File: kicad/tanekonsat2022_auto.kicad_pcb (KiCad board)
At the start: 2 copper layers, 79 x 68 mm, 102 parts, among them IC1 W25Q128JVSIQ, IC2 ADP3338AKCZ-3.3-RL, IC4 TESEO-LIV3F, IC5 CGGBPD.25.A, IC6 MAX2641EUT+T, IC7 TB67H450FNG,EL, IC8 TB67H450FNG,EL, J1 Conn_01x02_Male, J10 Conn_01x05_Female, J11 Conn_01x02_Female, J2 USB_B_Micro, J3 Conn_01x02_Male, J4 Conn_01x02_Male, J5 Conn_01x04_Male, J6 Conn_01x04_Male, J7 Conn_01x04_Female, J8 Conn_01x02_Female, J9 Conn_01x05_Female, M1 Motor_DC, M2 Motor_DC, Q1 Q_NMOS_DGS, Q2 Q_NMOS_DGS, Q7 Q_NMOS_DGS, SW1 SW_DIP_x01, U1 RP2040, U2 CR1025, U5 LT6106, U6 Opamp_Dual, Y1 SIT2001BI-S2-33E-12.000000D, Y2 FC-135_32.768KHz_7pF_+_-20ppm

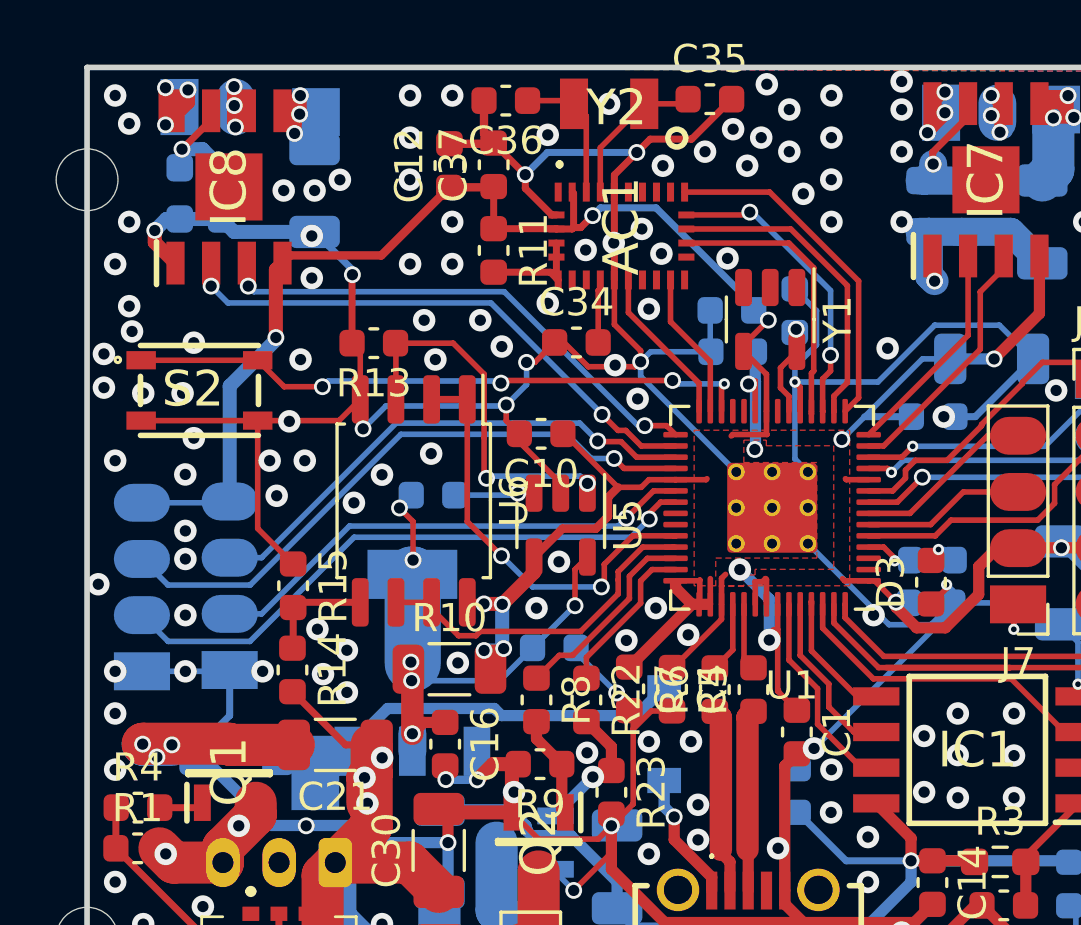
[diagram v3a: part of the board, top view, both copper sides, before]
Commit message: panelized main board
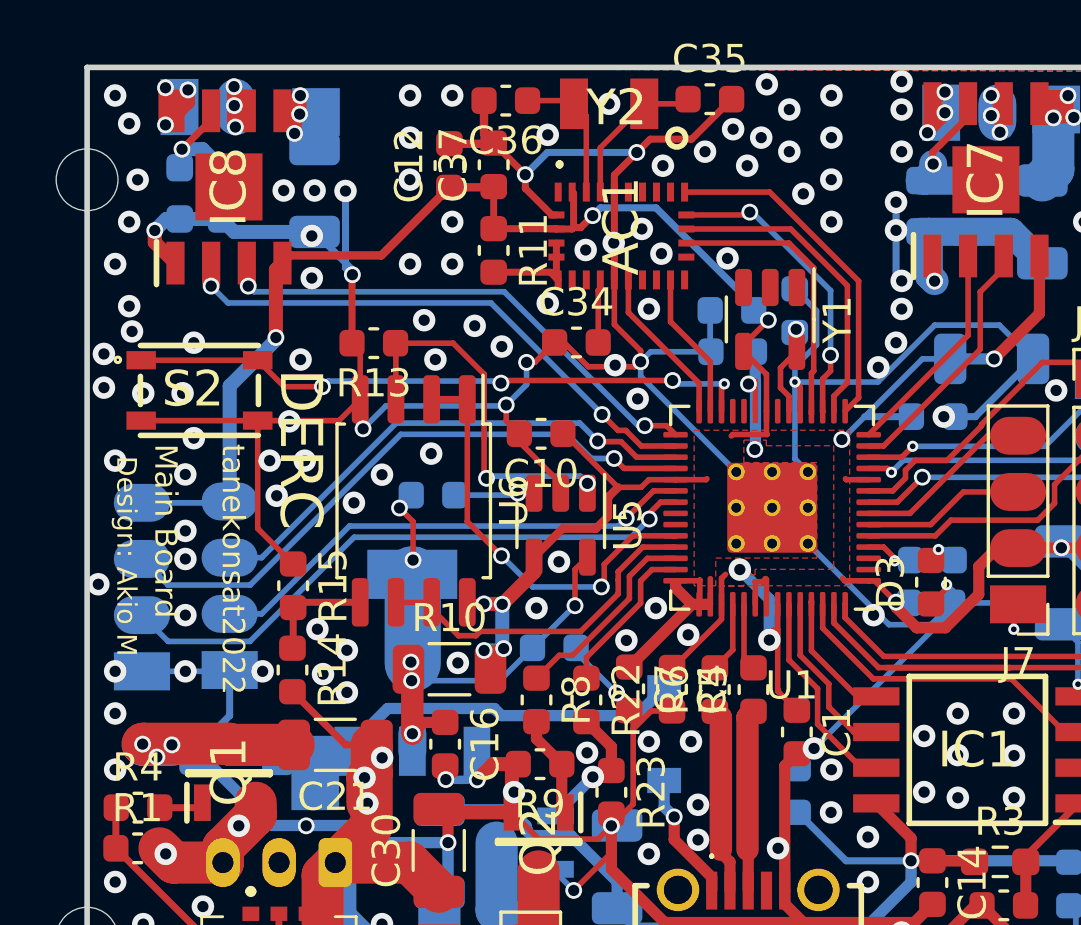
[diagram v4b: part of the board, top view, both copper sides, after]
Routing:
- net GND: track 296.3 -> 302.3 mm, vias 280 -> 285
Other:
- board text added: "Main Board"
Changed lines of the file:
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@@
       (effects (font (size 1 1) (thickness 0.15)) (justify mirror))
     )
-    (fp_text value "R" (at 0 -1.43 90) (layer "B.Fab")
+    (fp_text value "R" (at -0.6 -1.43 90) (layer "B.Fab")
       (effects (font (size 1 1) (thickness 0.15)) (justify mirror))
     )
@@
       (effects (font (size 1 1) (thickness 0.15)) (justify mirror))
     )
+    (fp_line (start -1.33 1.33) (end 0 1.33) (layer "B.SilkS") (width 0.12))
+    (fp_line (start -1.33 -1.27) (end -1.33 -1.33) (layer "B.SilkS") (width 0.12))
     (fp_line (start -1.33 0) (end -1.33 1.33) (layer "B.SilkS") (width 0.12))
-    (fp_line (start -1.33 -1.27) (end -1.33 -1.33) (layer "B.SilkS") (width 0.12))
-    (fp_line (start -1.33 1.33) (end 0 1.33) (layer "B.SilkS") (width 0.12))
+    (fp_line (start 1.33 -1.27) (end 1.33 -1.33) (layer "B.SilkS") (width 0.12))
     (fp_line (start -1.33 -1.27) (end 1.33 -1.27) (layer "B.SilkS") (width 0.12))
     (fp_line (start -1.33 -1.33) (end 1.33 -1.33) (layer "B.SilkS") (width 0.12))
-    (fp_line (start 1.33 -1.27) (end 1.33 -1.33) (layer "B.SilkS") (width 0.12))
     (fp_line (start -1.8 1.8) (end -1.8 -1.8) (layer "B.CrtYd") (width 0.05))
+    (fp_line (start 1.8 1.8) (end -1.8 1.8) (layer "B.CrtYd") (width 0.05))
     (fp_line (start 1.8 -1.8) (end 1.8 1.8) (layer "B.CrtYd") (width 0.05))
     (fp_line (start -1.8 -1.8) (end 1.8 -1.8) (layer "B.CrtYd") (width 0.05))
-    (fp_line (start 1.8 1.8) (end -1.8 1.8) (layer "B.CrtYd") (width 0.05))
     (fp_line (start 1.27 1.27) (end 1.27 -1.27) (layer "B.Fab") (width 0.1))
+    (fp_line (start -0.635 1.27) (end 1.27 1.27) (layer "B.Fab") (width 0.1))
+    (fp_line (start -1.27 0.635) (end -0.635 1.27) (layer "B.Fab") (width 0.1))
     (fp_line (start -1.27 -1.27) (end -1.27 0.635) (layer "B.Fab") (width 0.1))
-    (fp_line (start -1.27 0.635) (end -0.635 1.27) (layer "B.Fab") (width 0.1))
-    (fp_line (start -0.635 1.27) (end 1.27 1.27) (layer "B.Fab") (width 0.1))
     (fp_line (start 1.27 -1.27) (end -1.27 -1.27) (layer "B.Fab") (width 0.1))
     (pad "1" smd rect (at 0 0 180) (size 1.7 1.7) (layers "B.Cu" "B.Paste" "B.Mask")
@@
     (effects (font (size 0.8 0.8) (thickness 0.15)) (justify left))
   )
+  (gr_text "Design: Akio M" (at 104.4 75.4 270) (layer "F.SilkS")
+    (effects (font (size 0.7 0.7) (thickness 0.15)))
+  )
   (gr_text "I2C" (at 179.8574 54.1528) (layer "F.SilkS")
     (effects (font (size 1 1) (thickness 0.2)))
   )
+  (gr_text "DERC" (at 110.6 71.6 270) (layer "F.SilkS")
+    (effects (font (size 1.5 1.5) (thickness 0.3)))
+  )
   (gr_text "UART" (at 179.324 31.4) (layer "F.SilkS")
     (effects (font (size 1 1) (thickness 0.2)))
@@
     (effects (font (size 0.7 0.7) (thickness 0.15)))
   )
+  (gr_text "tanekonsat2022" (at 108.2 71.4 270) (layer "F.SilkS")
+    (effects (font (size 0.8 0.8) (thickness 0.15)) (justify left))
+  )
   (gr_text "Design: Akio M" (at 154.94 55.372) (layer "F.SilkS")
     (effects (font (size 0.7 0.7) (thickness 0.15)))
   )
   (gr_text "tanekonsat2022" (at 150.876 51.054) (layer "F.SilkS")
+    (effects (font (size 0.8 0.8) (thickness 0.15)) (justify left))
+  )
+  (gr_text "Main Board" (at 105.8 71.4 270) (layer "F.SilkS")
     (effects (font (size 0.8 0.8) (thickness 0.15)) (justify left))
   )
@@
   (via (at 104 87) (size 0.8) (drill 0.4) (layers "F.Cu" "B.Cu") (free) (net 2))
   (via (at 175.26 43.18) (size 0.8) (drill 0.4) (layers "F.Cu" "B.Cu") (free) (net 2))
-  (via (at 131.5 68) (size 0.8) (drill 0.4) (layers "F.Cu" "B.Cu") (free) (net 2))
+  (via (at 131.8 67.8) (size 0.8) (drill 0.4) (layers "F.Cu" "B.Cu") (free) (net 2))
   (via (at 134.8 92) (size 0.8) (drill 0.4) (layers "F.Cu" "B.Cu") (free) (net 2))
   (via (at 180.7 38.2) (size 0.8) (drill 0.4) (layers "F.Cu" "B.Cu") (free) (net 2))
@@
   (via (at 118.64647 68.50073) (size 0.6) (drill 0.4) (layers "F.Cu" "B.Cu") (net 2))
   (via (at 127.6 85.8) (size 0.8) (drill 0.4) (layers "F.Cu" "B.Cu") (free) (net 2))
-  (via (at 132 63.5) (size 0.8) (drill 0.4) (layers "F.Cu" "B.Cu") (free) (net 2))
+  (via (at 131.8 63.8) (size 0.8) (drill 0.4) (layers "F.Cu" "B.Cu") (free) (net 2))
   (via (at 103.6 68.2) (size 0.8) (drill 0.4) (layers "F.Cu" "B.Cu") (free) (net 2))
+  (via (at 132 65.6) (size 0.8) (drill 0.4) (layers "F.Cu" "B.Cu") (free) (net 2))
   (via (at 167.386 49.53) (size 0.8) (drill 0.4) (layers "F.Cu" "B.Cu") (free) (net 2))
   (via (at 180.34 48.26) (size 0.8) (drill 0.4) (layers "F.Cu" "B.Cu") (free) (net 2))
@@
   (via (at 177.165 55.88) (size 0.8) (drill 0.4) (layers "F.Cu" "B.Cu") (free) (net 2))
   (via (at 123.5 61.5) (size 0.8) (drill 0.4) (layers "F.Cu" "B.Cu") (free) (net 2))
-  (via (at 112 62) (size 0.8) (drill 0.4) (layers "F.Cu" "B.Cu") (free) (net 2))
+  (via (at 112.2 62.4) (size 0.8) (drill 0.4) (layers "F.Cu" "B.Cu") (free) (net 2))
   (via (at 160.00721 41.892848) (size 0.8) (drill 0.4) (layers "F.Cu" "B.Cu") (free) (net 2))
   (via (at 109.25 79.5) (size 0.8) (drill 0.4) (layers "F.Cu" "B.Cu") (free) (net 2))
@@
   (via (at 126 92) (size 0.8) (drill 0.4) (layers "F.Cu" "B.Cu") (free) (net 2))
   (via (at 106.8 71.2) (size 0.8) (drill 0.4) (layers "F.Cu" "B.Cu") (free) (net 2))
+  (via (at 132 66.6) (size 0.8) (drill 0.4) (layers "F.Cu" "B.Cu") (free) (net 2))
   (via (at 136 81) (size 0.8) (drill 0.4) (layers "F.Cu" "B.Cu") (free) (net 2))
   (via (at 169.672 48.768) (size 0.8) (drill 0.4) (layers "F.Cu" "B.Cu") (free) (net 2))
@@
   (via (at 132 58.5) (size 0.8) (drill 0.4) (layers "F.Cu" "B.Cu") (free) (net 2))
   (via (at 106.321488 92) (size 0.8) (drill 0.4) (layers "F.Cu" "B.Cu") (free) (net 2))
-  (via (at 117 67) (size 0.8) (drill 0.4) (layers "F.Cu" "B.Cu") (free) (net 2))
+  (via (at 116.8 67.2) (size 0.8) (drill 0.4) (layers "F.Cu" "B.Cu") (free) (net 2))
   (via (at 162.56 41.91) (size 0.8) (drill 0.4) (layers "F.Cu" "B.Cu") (free) (net 2))
   (via (at 106.8 67.8) (size 0.8) (drill 0.4) (layers "F.Cu" "B.Cu") (free) (net 2))
@@
   (via (at 152.4 55.88) (size 0.8) (drill 0.4) (layers "F.Cu" "B.Cu") (free) (net 2))
   (via (at 104.6 67.4) (size 0.8) (drill 0.4) (layers "F.Cu" "B.Cu") (free) (net 2))
+  (via (at 131.167551 68.677566) (size 0.8) (drill 0.4) (layers "F.Cu" "B.Cu") (free) (net 2))
   (via (at 104 83) (size 0.8) (drill 0.4) (layers "F.Cu" "B.Cu") (free) (net 2))
   (via (at 160.02 53.34) (size 0.8) (drill 0.4) (layers "F.Cu" "B.Cu") (free) (net 2))
@@
   (via (at 167.64 41.656) (size 0.8) (drill 0.4) (layers "F.Cu" "B.Cu") (free) (net 2))
   (via (at 152.4 26.67) (size 0.8) (drill 0.4) (layers "F.Cu" "B.Cu") (free) (net 2))
+  (via (at 131.8 62.8) (size 0.8) (drill 0.4) (layers "F.Cu" "B.Cu") (free) (net 2))
   (via (at 177.8 43.18) (size 0.8) (drill 0.4) (layers "F.Cu" "B.Cu") (free) (net 2))
   (via (at 107 90.5) (size 0.8) (drill 0.4) (layers "F.Cu" "B.Cu") (free) (net 2))
@@
   (via (at 132.8 81.8) (size 0.8) (drill 0.4) (layers "F.Cu" "B.Cu") (free) (net 2))
   (via (at 129.5 83) (size 0.8) (drill 0.4) (layers "F.Cu" "B.Cu") (free) (net 2))
+  (via (at 104.8 62) (size 0.8) (drill 0.4) (layers "F.Cu" "B.Cu") (free) (net 2))
   (via (at 123 66.6) (size 0.8) (drill 0.4) (layers "F.Cu" "B.Cu") (free) (net 2))
   (via (at 118 92.5195) (size 0.8) (drill 0.4) (layers "F.Cu" "B.Cu") (free) (net 2))
@@
   (segment (start 131.153862 69.2) (end 133.176582 67.17728) (width 0.2) (layer "B.Cu") (net 2))
   (segment (start 117.88623 70.0532) (end 113.6396 70.0532) (width 0.2) (layer "B.Cu") (net 2))
+  (segment (start 131.8 63.8) (end 131.8 65.4) (width 0.25) (layer "B.Cu") (net 2))
   (segment (start 108.031 79.5) (end 108.077 79.454) (width 0.2) (layer "B.Cu") (net 2))
   (segment (start 121.666 85) (end 121.8558 85) (width 0.2) (layer "B.Cu") (net 2))
@@
   (segment (start 122.7074 68.4784) (end 123.063 68.1228) (width 0.2) (layer "B.Cu") (net 2))
   (segment (start 117.921858 70.017572) (end 117.88623 70.0532) (width 0.2) (layer "B.Cu") (net 2))
+  (segment (start 112.2 62.4) (end 112.2 65.1338) (width 0.25) (layer "B.Cu") (net 2))
   (segment (start 138.2776 78.4606) (end 137.6426 77.8256) (width 0.2) (layer "B.Cu") (net 2))
   (segment (start 133.04568 77.83812) (end 131.54882 77.83812) (width 0.2) (layer "B.Cu") (net 2))
@@
   (segment (start 115.5446 89.076) (end 115.5446 87.3778) (width 1.5) (layer "B.Cu") (net 2))
   (segment (start 128.880278 82.244522) (end 133.8202 77.3046) (width 0.2) (layer "B.Cu") (net 2))
+  (segment (start 131.8 65.4) (end 132 65.6) (width 0.25) (layer "B.Cu") (net 2))
   (segment (start 112.4458 65.3796) (end 112.4458 65.2036) (width 0.25) (layer "B.Cu") (net 2))
   (segment (start 126.1126 74.9519) (end 128.6626 72.4019) (width 0.5) (layer "B.Cu") (net 2))
@@
   (segment (start 126.1126 72.4019) (end 128.6626 72.4019) (width 0.5) (layer "B.Cu") (net 2))
   (segment (start 119.6782 86.548) (end 119.6782 86.6533) (width 0.2) (layer "B.Cu") (net 2))
+  (segment (start 112.2 65.1338) (end 112.4458 65.3796) (width 0.25) (layer "B.Cu") (net 2))
   (segment (start 121.8558 85) (end 121.8692 84.9866) (width 0.2) (layer "B.Cu") (net 2))
   (segment (start 125.1836 66.6496) (end 125.1836 68.0974) (width 0.2) (layer "B.Cu") (net 2))
@@
   (segment (start 132.9671 63.8537) (end 134.1374 63.8537) (width 1) (layer "B.Cu") (net 2))
   (segment (start 128.96832 66.66152) (end 128.1938 65.887) (width 0.2) (layer "B.Cu") (net 2))
+  (segment (start 131.8 63.8) (end 131.8 62.8) (width 0.25) (layer "B.Cu") (net 2))
   (segment (start 127.3876 72.4019) (end 128.6626 72.4019) (width 0.2) (layer "B.Cu") (net 2))
   (segment (start 115.8494 87.073) (end 115.5446 87.3778) (width 0.4) (layer "B.Cu") (net 2))

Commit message: update conn
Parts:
- removed J2: USB_B_Micro, SamacSys_Parts:101181940001LFBKN
- added R16: 5.1k, Resistor_SMD:R_0603_1608Metric, B.Cu at (127.7, 88.7)
- added R17: 5.1k, Resistor_SMD:R_0603_1608Metric, B.Cu at (125.0, 88.6)
- added U4: USB_type_C, tanekonsat:USB_typeC_t, F.Cu at (121.9, 85.9)
- moved C17 6.80 mm to (126.2, 91.7), turned to 0 degrees
- moved C16 4.24 mm to (112.3, 79.6)
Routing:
- net GND: track 302.3 -> 433.4 mm, vias 285 -> 283
- net +3V3: track 152.2 -> 214.7 mm, vias 12 -> 19
- net /VBUS: track 4.62 -> 11.0 mm
- net /3V3_REG_OUT: track 19.9 -> 24.9 mm, vias 6 -> 7
- net Net-(R16-Pad1): track 0.00 -> 2.22 mm, vias 0 -> 1
- net Net-(R17-Pad1): track 0.00 -> 1.88 mm, vias 0 -> 1
- net /RUN: track 22.4 -> 24.0 mm
- net /USB_D-: track 6.60 -> 7.64 mm
- net /+7V4: track 66.0 -> 65.1 mm
- net /GPIO26_ADC_I_monitor: track 15.2 -> 16.0 mm
- net GND1: vias 0 -> 1
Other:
- board text added: "BAT 7.4V"
- board text added: "BOOT"
- board text added: "RUN"
